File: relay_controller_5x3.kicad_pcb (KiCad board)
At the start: 2 copper layers, 118.1 x 55.1 mm, 46 parts, among them P1 PWR_JACK_2.5x5.5, P2 HEADER_01X03_SMD_RA, P3 HEADER_01X03_SMD_RA, P4 HEADER_01X03_SMD_RA, P5 HEADER_01X03_SMD_RA, P6 HEADER_01X02_SMD_RA, P7 BNC_DOUBLE_RA, SW1 SPST_SLIDE_AS, T1 TERM_BLK_ANG_2_PIN, T2 TERM_BLK_ANG_2_PIN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

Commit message: Progress towards v1.2.
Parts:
- added D1: diode_schottky_45V_10A, relay_controller_5x3:CFP15, F.Cu at (201.9, 113.7)
- REG1: value CONV_DC_DC_12V_1A -> CONV_DC_DC_9V_1A
- T1, T2, T3, T4, T5, T6, T7, T8: value TERM_BLK_ANG_2_PIN -> TERM_BLK_ANG_2_PIN_0.2_PITCH; footprint relay_controller_5x3:TERM_BLK_ANG_2_PIN -> relay_controller_5x3:TERM_BLK_ANG_2_PIN_0.2_PITCH
- moved SW1 18.5 mm to (201.3, 94.0)
- moved L1 15.4 mm to (200.0, 109.2), turned to 270 degrees
- moved L2 13.6 mm to (113.7, 89.5), turned to 180 degrees
- moved L3 13.6 mm to (134.0, 89.5), turned to 180 degrees
- moved L4 13.6 mm to (154.3, 89.5), turned to 180 degrees
- moved L5 13.6 mm to (174.6, 89.5), turned to 180 degrees
- moved L6 13.6 mm to (113.7, 111.1), turned to 180 degrees
- moved L7 13.6 mm to (134.0, 111.1), turned to 180 degrees
- moved L8 13.6 mm to (154.3, 111.1), turned to 180 degrees
- moved L9 13.6 mm to (174.6, 111.1), turned to 180 degrees
- moved C1 10.2 mm to (201.3, 98.4)
- moved U5 8.26 mm to (120.0, 116.8), turned to 90 degrees
- moved U6 8.26 mm to (140.3, 116.8), turned to 90 degrees
- moved U7 8.26 mm to (160.7, 116.8), turned to 90 degrees
- moved U8 8.26 mm to (181.0, 116.8), turned to 90 degrees
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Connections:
- net /RELAY_0 renamed /SIGNAL_0
- net /RELAY_1 renamed /SIGNAL_1
- net /RELAY_2 renamed /SIGNAL_2
- net /RELAY_3 renamed /SIGNAL_3
- net /RELAY_4 renamed /SIGNAL_4
- net /RELAY_5 renamed /SIGNAL_5
- net /RELAY_6 renamed /SIGNAL_6
- net /RELAY_7 renamed /SIGNAL_7
- ARDUINO1 pad 2: (no net) -> /BNC_A
- ARDUINO1 pad 48: /BNC_A -> (no net)
- P6 pad 2: VAA -> VCC
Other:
- board text added: "+12-42VDC"
- board text added: "9V"
- board text added: "Janelia Modular Device relay_controller_5x3 part_number: 1190 01/2017 ver 1.2"
- board text removed: "+24VDC"
- board text removed: "12V"
- board text removed: "Janelia Modular Device relay_controller_5x3 model_number: 1190 04/2016 ver 1.1"

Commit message: Added signal outputs.
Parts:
- added S1: HEADER_01X02_SMD, relay_controller_5x3:Header_2_Pin_SMD, F.Cu at (120.0, 97.2)
- added S2: HEADER_01X02_SMD, relay_controller_5x3:Header_2_Pin_SMD, F.Cu at (140.3, 97.2)
- added S3: HEADER_01X02_SMD, relay_controller_5x3:Header_2_Pin_SMD, F.Cu at (160.7, 97.2)
- added S4: HEADER_01X02_SMD, relay_controller_5x3:Header_2_Pin_SMD, F.Cu at (180.3, 97.2)
- added S5: HEADER_01X02_SMD, relay_controller_5x3:Header_2_Pin_SMD, F.Cu at (120.0, 118.7)
- added S6: HEADER_01X02_SMD, relay_controller_5x3:Header_2_Pin_SMD, F.Cu at (140.3, 118.7)
- added S7: HEADER_01X02_SMD, relay_controller_5x3:Header_2_Pin_SMD, F.Cu at (160.7, 118.7)
- added S8: HEADER_01X02_SMD, relay_controller_5x3:Header_2_Pin_SMD, F.Cu at (181.0, 118.7)

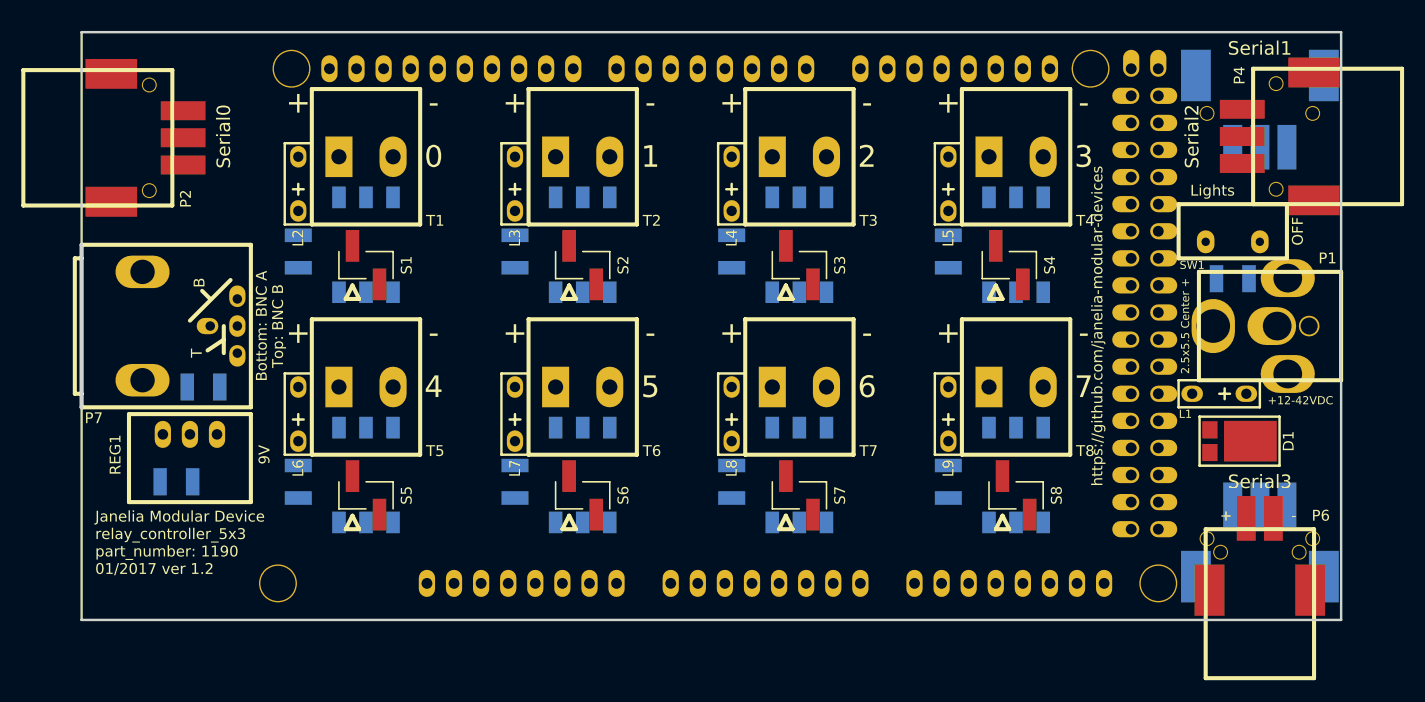
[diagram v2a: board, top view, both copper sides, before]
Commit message: Changed to shrouded headers.
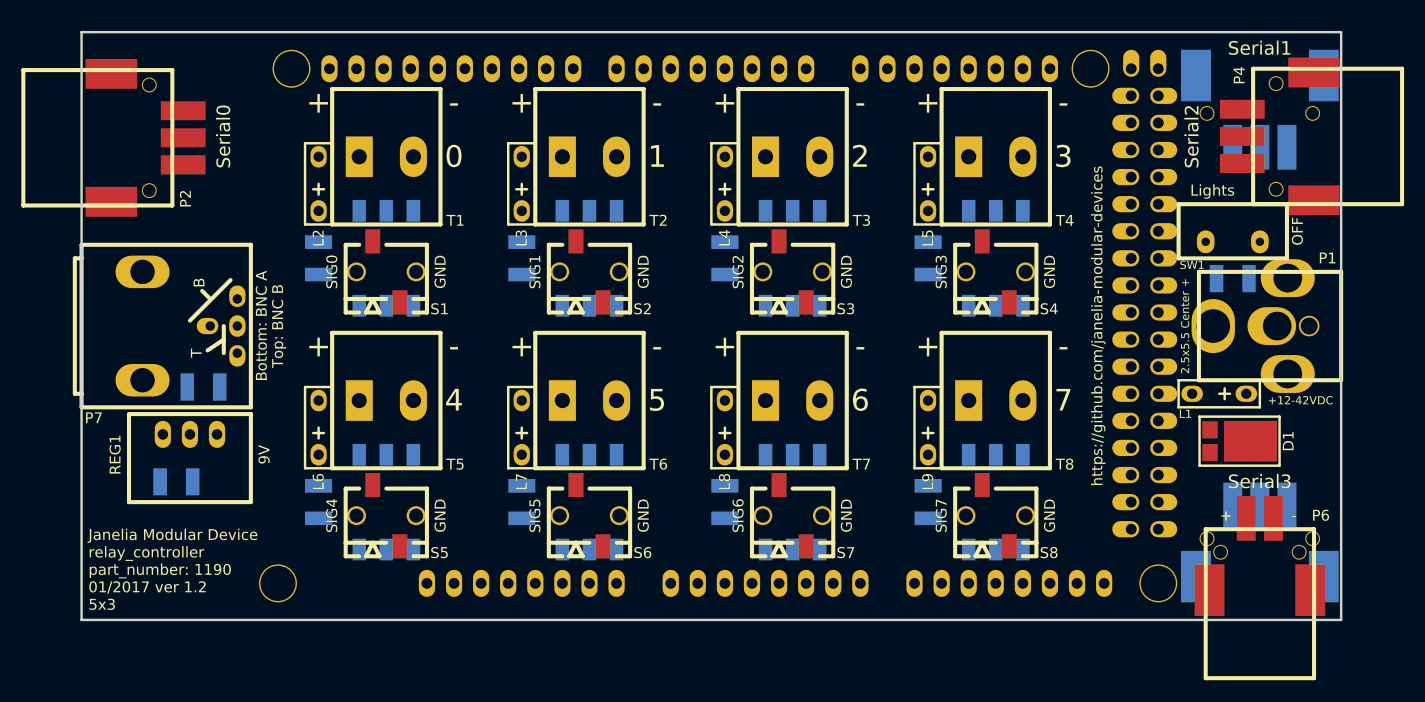
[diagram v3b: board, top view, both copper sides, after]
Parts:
- S1, S2, S3, S4, S5, S6, S7, S8: value HEADER_01X02_SMD -> HEADER_01X02_SMD_SHR; footprint relay_controller_5x3:Header_2_Pin_SMD -> relay_controller_5x3:Header_2_Pin_SMD_SHR
- moved U5 3.17 mm to (121.9, 119.4)
- moved U8 3.17 mm to (179.1, 119.4)
- moved R8 2.69 mm to (172.7, 119.4)
- moved S5 2.69 mm to (121.9, 120.7)
- moved S8 2.69 mm to (179.1, 120.7)
- moved R5 2.69 mm to (115.6, 119.4)
- moved U6 2.62 mm to (141.0, 119.4)
- moved U7 2.62 mm to (160.0, 119.4)
- moved T5 2.29 mm to (121.9, 109.9)
- moved T8 2.29 mm to (179.1, 109.9)
- moved L9 2.29 mm to (172.7, 112.4)
- moved U1 2.29 mm to (121.9, 96.5)
- moved U4 2.29 mm to (179.1, 96.5)
- moved L6 2.29 mm to (115.6, 112.4)
- moved R7 2.01 mm to (153.7, 119.4)
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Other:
- board text added: "GND"
- board text added: "Janelia Modular Device relay_controller part_number: 1190 01/2017 ver 1.2 5x3"
- board text added: "SIG0"
- board text added: "SIG1"
- board text added: "SIG2"
- board text added: "SIG3"
- board text added: "SIG4"
- board text added: "SIG5"
- board text added: "SIG6"
- board text added: "SIG7"
- board text removed: "Janelia Modular Device relay_controller_5x3 part_number: 1190 01/2017 ver 1.2"

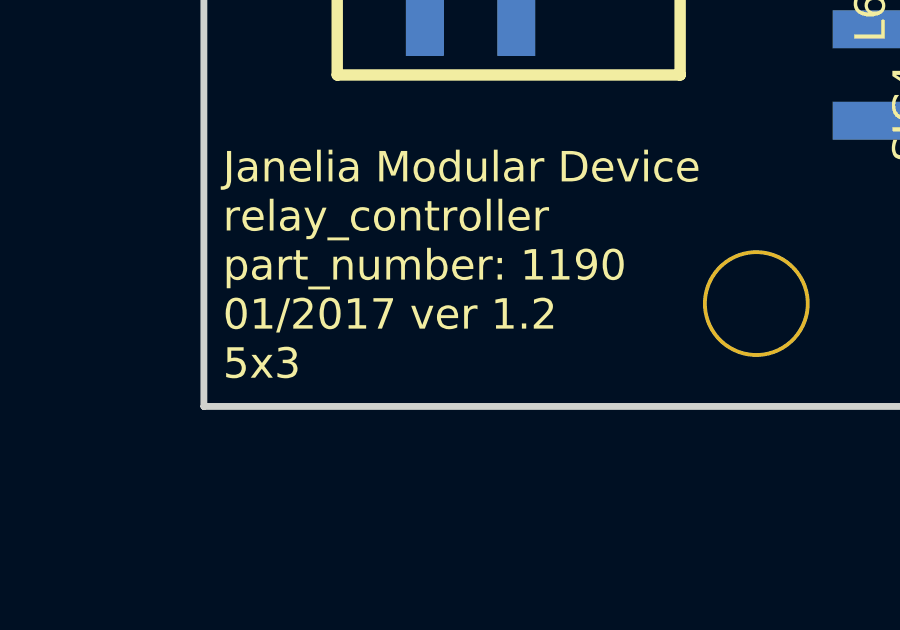
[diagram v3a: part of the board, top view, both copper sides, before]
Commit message: Updated relays and resistors.
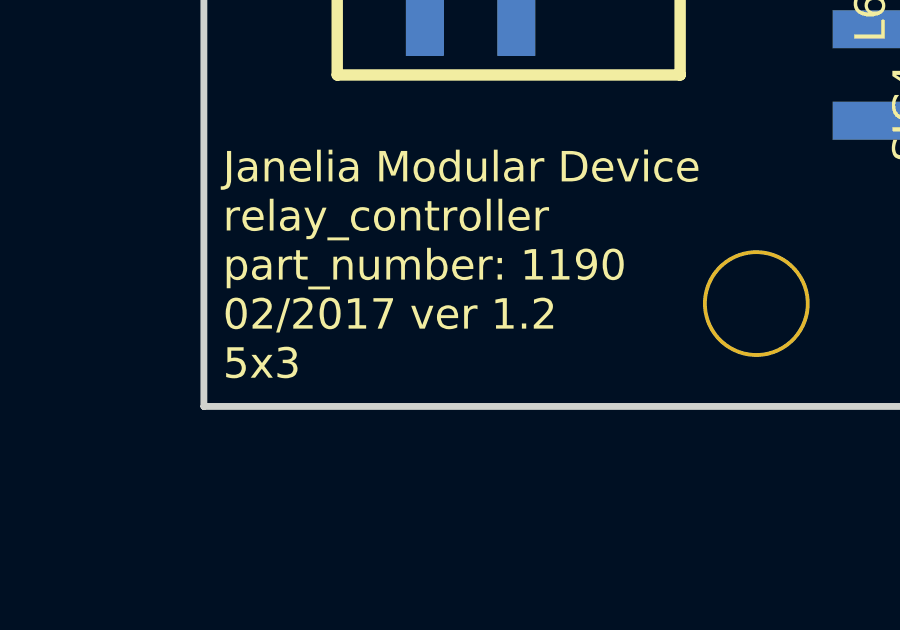
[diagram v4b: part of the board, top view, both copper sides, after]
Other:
- board text added: "Janelia Modular Device relay_controller part_number: 1190 02/2017 ver 1.2 5x3"
- board text removed: "Janelia Modular Device relay_controller part_number: 1190 01/2017 ver 1.2 5x3"
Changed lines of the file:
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@@
-(kicad_pcb (version 20160815) (host pcbnew no-vcs-found-7475~57~ubuntu16.04.1)
+(kicad_pcb (version 20170123) (host pcbnew no-vcs-found-7560~57~ubuntu16.04.1)
   (general
     (links 114)
     (no_connects 114)
-    (area 93.230699 75.196699 211.569301 130.543301)
+    (area 87.439499 70.675499 218.374686 136.334501)
     (thickness 1.6)
     (drawings 56)
@@
   (module relay_controller_5x3:Header_2_Pin_SMD_SHR (layer F.Cu)
     (at 121.92 97.79 180)
-    (fp_text reference S1 (at -5 -3.5 360) (layer F.SilkS)
-      (effects (font (size 1.016 1.016) (thickness 0.254)))
-    )
-    (fp_text value HEADER_01X02_SMD_SHR (at 5 -3.5 360) (layer F.SilkS) hide
+    (fp_text reference S1 (at -5 -3.5) (layer F.SilkS)
+      (effects (font (size 1.016 1.016) (thickness 0.254)))
+    )
+    (fp_text value HEADER_01X02_SMD_SHR (at 5 -3.5) (layer F.SilkS) hide
       (effects (font (thickness 0.3048)))
     )
@@
   (module relay_controller_5x3:Header_2_Pin_SMD_SHR (layer F.Cu)
     (at 140.97 97.79 180)
-    (fp_text reference S2 (at -5 -3.5 360) (layer F.SilkS)
-      (effects (font (size 1.016 1.016) (thickness 0.254)))
-    )
-    (fp_text value HEADER_01X02_SMD_SHR (at 5 -3.5 360) (layer F.SilkS) hide
+    (fp_text reference S2 (at -5 -3.5) (layer F.SilkS)
+      (effects (font (size 1.016 1.016) (thickness 0.254)))
+    )
+    (fp_text value HEADER_01X02_SMD_SHR (at 5 -3.5) (layer F.SilkS) hide
       (effects (font (thickness 0.3048)))
     )
@@
   (module relay_controller_5x3:Header_2_Pin_SMD_SHR (layer F.Cu)
     (at 160.02 97.79 180)
-    (fp_text reference S3 (at -5 -3.5 360) (layer F.SilkS)
-      (effects (font (size 1.016 1.016) (thickness 0.254)))
-    )
-    (fp_text value HEADER_01X02_SMD_SHR (at 5 -3.5 360) (layer F.SilkS) hide
+    (fp_text reference S3 (at -5 -3.5) (layer F.SilkS)
+      (effects (font (size 1.016 1.016) (thickness 0.254)))
+    )
+    (fp_text value HEADER_01X02_SMD_SHR (at 5 -3.5) (layer F.SilkS) hide
       (effects (font (thickness 0.3048)))
     )
@@
   (module relay_controller_5x3:Header_2_Pin_SMD_SHR (layer F.Cu)
     (at 179.07 97.79 180)
-    (fp_text reference S4 (at -5 -3.5 360) (layer F.SilkS)
-      (effects (font (size 1.016 1.016) (thickness 0.254)))
-    )
-    (fp_text value HEADER_01X02_SMD_SHR (at 5 -3.5 360) (layer F.SilkS) hide
+    (fp_text reference S4 (at -5 -3.5) (layer F.SilkS)
+      (effects (font (size 1.016 1.016) (thickness 0.254)))
+    )
+    (fp_text value HEADER_01X02_SMD_SHR (at 5 -3.5) (layer F.SilkS) hide
       (effects (font (thickness 0.3048)))
     )
@@
   (module relay_controller_5x3:Header_2_Pin_SMD_SHR (layer F.Cu)
     (at 121.92 120.65 180)
-    (fp_text reference S5 (at -5 -3.5 360) (layer F.SilkS)
-      (effects (font (size 1.016 1.016) (thickness 0.254)))
-    )
-    (fp_text value HEADER_01X02_SMD_SHR (at 5 -3.5 360) (layer F.SilkS) hide
+    (fp_text reference S5 (at -5 -3.5) (layer F.SilkS)
+      (effects (font (size 1.016 1.016) (thickness 0.254)))
+    )
+    (fp_text value HEADER_01X02_SMD_SHR (at 5 -3.5) (layer F.SilkS) hide
       (effects (font (thickness 0.3048)))
     )
@@
   (module relay_controller_5x3:Header_2_Pin_SMD_SHR (layer F.Cu)
     (at 140.97 120.65 180)
-    (fp_text reference S6 (at -5 -3.5 360) (layer F.SilkS)
-      (effects (font (size 1.016 1.016) (thickness 0.254)))
-    )
-    (fp_text value HEADER_01X02_SMD_SHR (at 5 -3.5 360) (layer F.SilkS) hide
+    (fp_text reference S6 (at -5 -3.5) (layer F.SilkS)
+      (effects (font (size 1.016 1.016) (thickness 0.254)))
+    )
+    (fp_text value HEADER_01X02_SMD_SHR (at 5 -3.5) (layer F.SilkS) hide
       (effects (font (thickness 0.3048)))
     )
@@
   (module relay_controller_5x3:Header_2_Pin_SMD_SHR (layer F.Cu)
     (at 160.02 120.65 180)
-    (fp_text reference S7 (at -5 -3.5 360) (layer F.SilkS)
-      (effects (font (size 1.016 1.016) (thickness 0.254)))
-    )
-    (fp_text value HEADER_01X02_SMD_SHR (at 5 -3.5 360) (layer F.SilkS) hide
+    (fp_text reference S7 (at -5 -3.5) (layer F.SilkS)
+      (effects (font (size 1.016 1.016) (thickness 0.254)))
+    )
+    (fp_text value HEADER_01X02_SMD_SHR (at 5 -3.5) (layer F.SilkS) hide
       (effects (font (thickness 0.3048)))
     )
@@
   (module relay_controller_5x3:Header_2_Pin_SMD_SHR (layer F.Cu)
     (at 179.07 120.65 180)
-    (fp_text reference S8 (at -5 -3.5 360) (layer F.SilkS)
-      (effects (font (size 1.016 1.016) (thickness 0.254)))
-    )
-    (fp_text value HEADER_01X02_SMD_SHR (at 5 -3.5 360) (layer F.SilkS) hide
+    (fp_text reference S8 (at -5 -3.5) (layer F.SilkS)
+      (effects (font (size 1.016 1.016) (thickness 0.254)))
+    )
+    (fp_text value HEADER_01X02_SMD_SHR (at 5 -3.5) (layer F.SilkS) hide
       (effects (font (thickness 0.3048)))
     )
@@
     (effects (font (size 1.016 1.016) (thickness 0.1905)))
   )
-  (gr_text "Janelia Modular Device\nrelay_controller\npart_number: 1190\n01/2017 ver 1.2\n5x3" (at 93.98 125.73) (layer F.SilkS)
+  (gr_text "Janelia Modular Device\nrelay_controller\npart_number: 1190\n02/2017 ver 1.2\n5x3" (at 93.98 125.73) (layer F.SilkS)
     (effects (font (size 1.016 1.016) (thickness 0.254)) (justify left))
   )

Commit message: Progress towards next version.
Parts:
- R1, R2, R3, R4, R5, R6, R7, R8: value 249 -> 200
- U1, U2, U3, U4, U5, U6, U7, U8: value SSR_DC_6PIN -> SSR_DC_6PIN_2.5A; footprint relay_controller_5x3:ASSR-1611 -> relay_controller_5x3:6-SMD-GW-0.3IN
- turned L1 to 90 degrees
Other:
- net class LEDPOWER: trace_width 0.508 -> 0.6096
- net class SUPERPOWER: trace_width 1.016 -> 1.2192

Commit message: Finished v1.2.
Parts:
- T1, T2, T3, T4, T5, T6, T7, T8: value TERM_BLK_ANG_2_PIN_0.2_PITCH -> TERM_BLK_HDR_2POS_VERT_0.2IN; footprint relay_controller_5x3:TERM_BLK_ANG_2_PIN_0.2_PITCH -> relay_controller_5x3:TERM_BLK_HDR_2POS_VERT_0.2IN
- U1, U2, U3, U4, U5, U6, U7, U8: value SSR_DC_6PIN_2.5A -> SSR
- moved R1 13.3 mm to (128.9, 96.5)
- moved R2 13.3 mm to (148.0, 96.5)
- moved R3 13.3 mm to (167.0, 96.5)
- moved R4 13.3 mm to (186.1, 96.5)
- moved R5 13.3 mm to (128.9, 119.4)
- moved R6 13.3 mm to (148.0, 119.4)
- moved R7 13.3 mm to (167.0, 119.4)
- moved R8 13.3 mm to (186.1, 119.4)
- moved L8 8.98 mm to (152.4, 121.3), turned to 0 degrees
- moved L3 8.35 mm to (133.3, 97.8), turned to 0 degrees
- moved L5 8.35 mm to (171.4, 97.8), turned to 0 degrees
- moved L7 8.35 mm to (133.3, 120.7), turned to 0 degrees
- moved L9 8.35 mm to (171.4, 120.7), turned to 0 degrees
- moved L2 8.35 mm to (114.3, 97.8), turned to 0 degrees
- moved L6 8.35 mm to (114.3, 120.7), turned to 0 degrees
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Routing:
- net GND: track 0.00 -> 459.0 mm
- net /LED_GND: track 0.00 -> 196.0 mm
- net VAA: track 0.00 -> 135.1 mm
- net /BNC_B: track 0.00 -> 80.8 mm
- net /SIGNAL_5: track 0.00 -> 78.3 mm
- net /SIGNAL_3: track 0.00 -> 76.8 mm
- net /TX3: track 0.00 -> 71.9 mm
- net /RX0: track 0.00 -> 70.0 mm
- net /BNC_A: track 0.00 -> 67.4 mm
- net /SIGNAL_4: track 0.00 -> 63.6 mm
- net /SIGNAL_6: track 0.00 -> 62.5 mm
- net /RX3: track 0.00 -> 61.1 mm
- net /TX0: track 0.00 -> 58.4 mm
- net /V_IN: track 0.00 -> 54.7 mm
- net /SIGNAL_0: track 0.00 -> 54.2 mm
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- added copper zone on B.Cu, net GND
- added copper zone on F.Cu, net GND
